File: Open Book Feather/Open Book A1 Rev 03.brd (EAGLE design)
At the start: 77.5 x 112.3 mm, 124 parts, among them J1 SJ-43514-SMT, J2 10118193-0001LF, Q1 DMG341, Q2 IRLML0100, SW1 SPDT_SWITCH, U1 AP2112-3.3, U2 MCP73831T-2ACI/OT, U3 ATSAMD51J64-TQFP(10X10), U4 GD25Q16C (or GD25Q32C), U5 MCP23008/SO, U6 GD25Q16C (or GD25Q32C), U8 MAX4466EXK+T, X1 JSTPH, X2 2x5 0.05" SWD

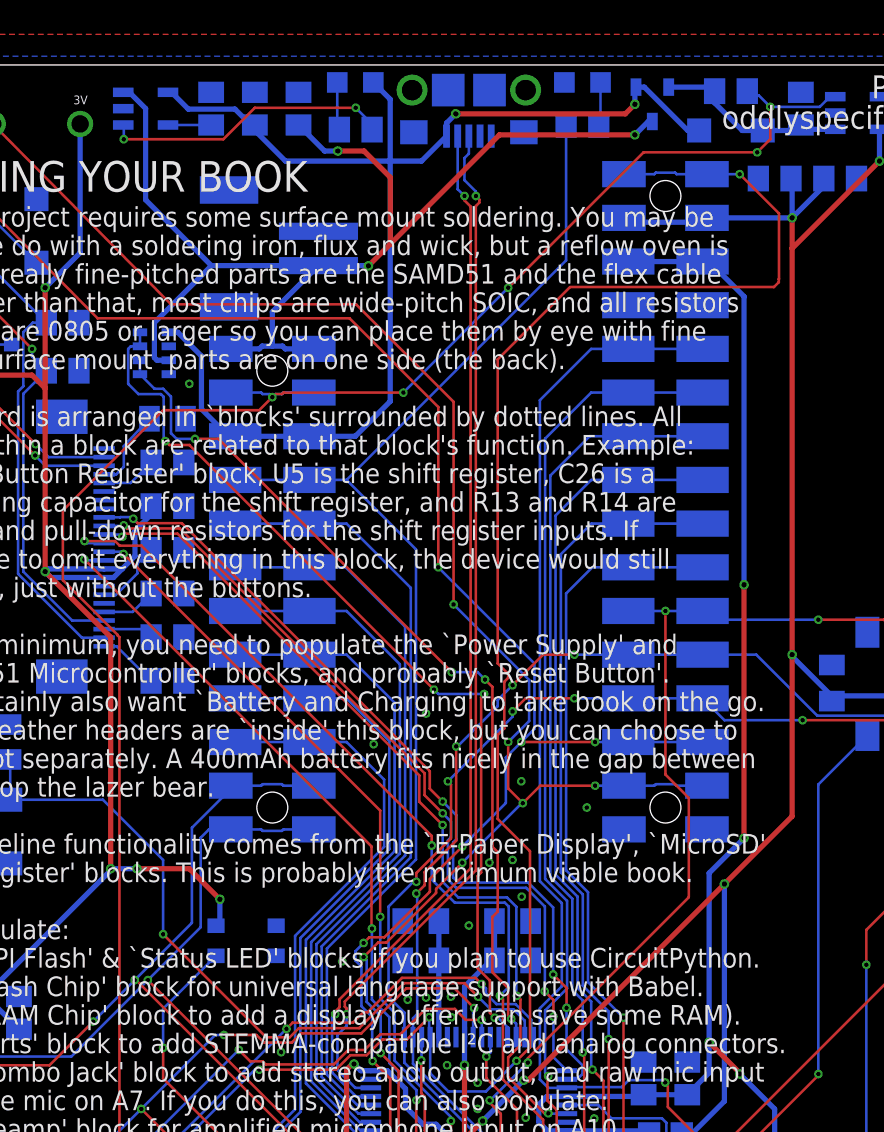
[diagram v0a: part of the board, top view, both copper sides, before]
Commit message: add indicator LED for full charge
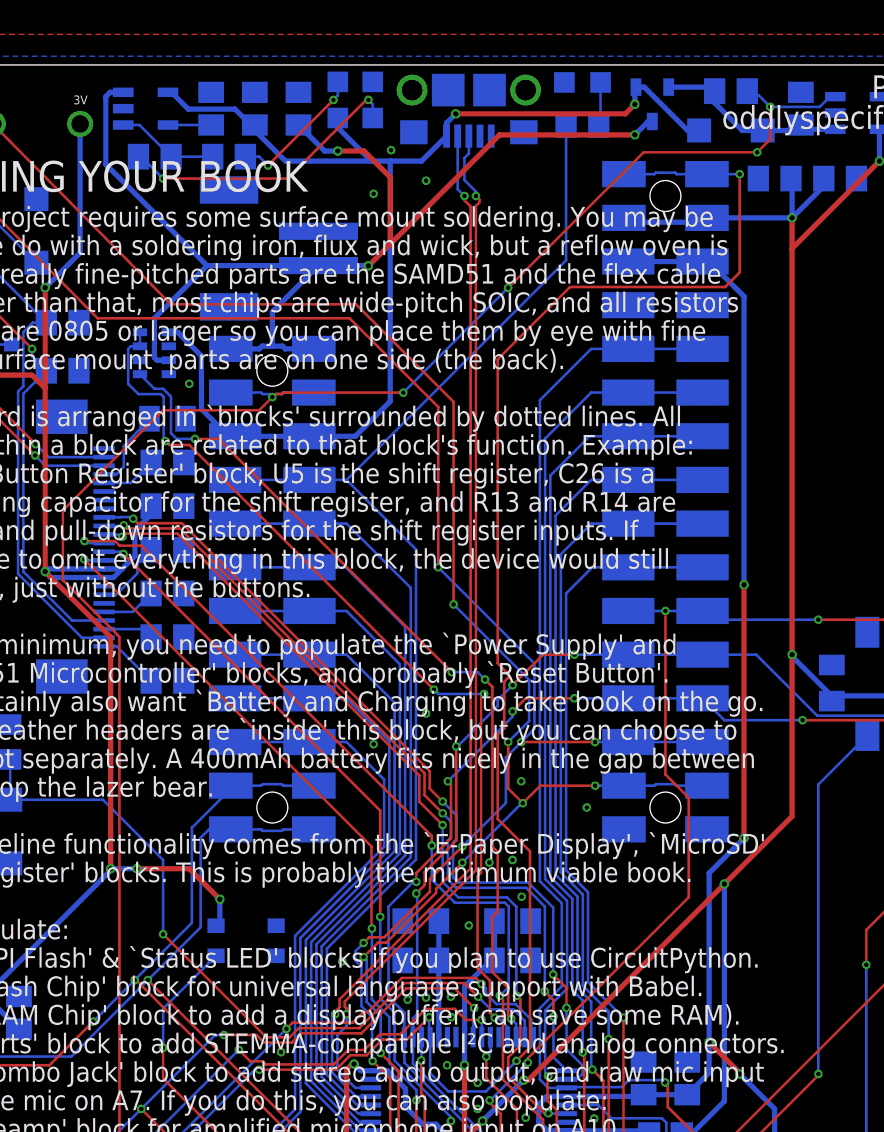
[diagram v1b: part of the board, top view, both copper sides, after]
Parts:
- added FUL: GREEN, adafruit:CHIP-LED0805
- added R8: 100, microbuilder:0805_10MGAP
- R5: value 10K -> 1K; device microbuilder:0805_10MGAP -> microbuilder:0805-NO
- R7: value 100 -> 10K
- moved R5 67.7 mm to (20.6, 106.9)
- moved R6 34.8 mm to (30.2, 39.9), turned to 180 degrees
- moved R4 7.53 mm to (24.9, 106.9), turned to 0 degrees
- moved R7 2.79 mm to (21.1, 6.35), turned to 270 degrees
- moved CHG 1.44 mm to (31.2, 110.2), turned to 0 degrees
- renumbered R27 to R9
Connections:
- removed net N$5: R4.2, U2.1
- new net N$6: FUL.A, R5.1
- new net STAT: R4.2, R5.2, U2.1
- net !RESET: now also R8.2; no longer R6.2
- net +3V3: now also R7.1; no longer R5.1
- net GND: now also FUL.C
- net N$1: now also R8.1; no longer R7.1
- net SWCLK: now also R6.2; no longer R5.2
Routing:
- net N$6: track 0.00 -> 16.9 mm, vias 0 -> 2
- net N$5: track 16.7 -> 0.00 mm, vias 2 -> 0
- net STAT: track 0.00 -> 5.97 mm
- net N$4: track 2.80 -> 8.06 mm, vias 0 -> 2
- net !RESET: track 162.3 -> 158.7 mm
- net VBUS: track 73.5 -> 71.9 mm
- net VBAT: track 70.4 -> 71.5 mm
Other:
- board text added: "An SWD connector (and test points) allow access to the serial wire debug interface. R6=SWCLK pullup"
- board text added: "BUTTON INPUT"
- board text added: "D1&Q1 conspire to let only the higher of VBAT & VBUS reach 3.3V regulator U1. C1 filters regulator input; C2 & C3 filter output. R1 pulls EN high to keep the regulator on. BATTERY: U2 is a LiPo charging controller. Powered by VBUS, it charges the battery at a rate determined by R3. C4=filter for VBAT, R4&R5 limit current to chg status LEDs. R9: voltage div to gauge VBAT & VBUS on A6/PB01 and A11/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"
- board text added: "Notes at end of the POWER SUPPLY block."
- board text added: "R7 pulls !RESET high. Btn pulls it low. C13 is a filter cap. R8 discharges C13. Double tap for UF2 bootloader."
- board text added: "See BUTTON INPUT."
- board text removed: "*Notes on this bit can be found at end of the POWER SUPPLY block."
- board text removed: "An SWD connector (and test points) allow access to the serial wire debug interface. R5=SWCLK pullup"
- board text removed: "D1&Q1 conspire to let only the higher of VBAT & VBUS reach 3.3V regulator U1. C1 filters regulator input; C2 & C3 filter output. R1 pulls EN high to keep the regulator on. BATTERY: U2 is a LiPo charging controller. Powered by VBUS, it charges the battery at a rate determined by R3. C4=filter for VBAT, R4 limits current to CHG LED. R8 & R9 are a voltage divider for VBAT to make a battery gauge on 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"
- board text removed: "GPIO EXPANDER"
- board text removed: "LOCK_BUTTON=D51=PA27"
- board text removed: "R6 pulls !RESET high. Btn pulls it low. C13 is a filter cap. R7 discharges C13. Double tap for UF2 bootloader."
